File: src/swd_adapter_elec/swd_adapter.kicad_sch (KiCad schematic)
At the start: 2 parts, among them J101 Conn_01x06_Pin, J102 Conn_01x14_Pin

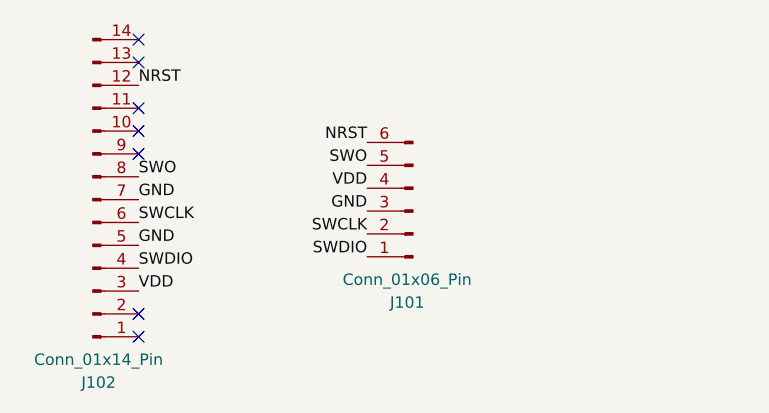
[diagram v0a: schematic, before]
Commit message: The IDC 14 pin to 6 pin converter
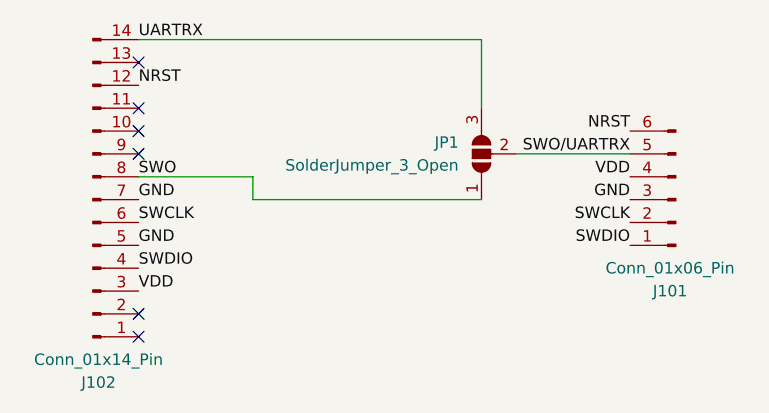
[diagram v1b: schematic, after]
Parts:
- added JP1: SolderJumper_3_Open, Jumper:SolderJumper-3_P1.3mm_Open_RoundedPad1.0x1.5mm, symbol Jumper:SolderJumper_3_Open
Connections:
- net SWO: now also JP1.1 (A); no longer J101.5 (Pin_5)
- net UARTRX: now reaches J102.14 (Pin_14)
- net UARTRX: now also JP1.3 (B)
- new net SWO/UARTRX: J101.5 (Pin_5), JP1.2 (C)
- no-connect marks 7 -> 6
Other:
- moved on the sheet: J101
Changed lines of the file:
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@@
-	)
-	(no_connect
-		(at 63.5 45.72)
 	)
 	(no_connect
 		(at 63.5 58.42)
 	)
+	(wire
+		(pts
+			(xy 105.41 58.42) (xy 118.11 58.42)
+		)
+		(stroke
+			(width 0)
+			(type default)
+		)
+	)
+	(wire
+		(pts
+			(xy 101.6 53.34) (xy 101.6 45.72)
+		)
+		(stroke
+			(width 0)
+			(type default)
+		)
+	)
+	(wire
+		(pts
+			(xy 63.5 45.72) (xy 101.6 45.72)
+		)
+		(stroke
+			(width 0)
+			(type default)
+		)
+	)
+	(wire
+		(pts
+			(xy 101.6 63.5) (xy 76.2 63.5)
+		)
+		(stroke
+			(width 0)
+			(type default)
+		)
+	)
+	(wire
+		(pts
+			(xy 63.5 60.96) (xy 76.2 60.96)
+		)
+		(stroke
+			(width 0)
+			(type default)
+		)
+	)
+	(wire
+		(pts
+			(xy 76.2 63.5) (xy 76.2 60.96)
+		)
+		(stroke
+			(width 0)
+			(type default)
+		)
+	)
 	(label "VDD"
-		(at 88.9 62.23 180)
+		(at 118.11 60.96 180)
 		(effects
 			(font
@@
 		)
 	)
-	(label "SWO"
-		(at 88.9 59.69 180)
+	(label "SWO{slash}UARTRX"
+		(at 118.11 58.42 180)
 		(effects
 			(font
@@
 	)
 	(label "SWCLK"
-		(at 88.9 67.31 180)
+		(at 118.11 66.04 180)
 		(effects
 			(font
@@
 		)
 	)
+	(label "UARTRX"
+		(at 63.5 45.72 0)
+		(effects
+			(font
+				(size 1.27 1.27)
+			)
+			(justify left bottom)
+		)
+	)
 	(label "SWDIO"
 		(at 63.5 71.12 0)
@@
 	)
 	(label "SWDIO"
-		(at 88.9 69.85 180)
+		(at 118.11 68.58 180)
 		(effects
 			(font
@@
 	)
 	(label "NRST"
-		(at 88.9 57.15 180)
+		(at 118.11 55.88 180)
 		(effects
 			(font
@@
 	)
 	(label "GND"
-		(at 88.9 64.77 180)
+		(at 118.11 63.5 180)
 		(effects
 			(font
@@
 	)
 	(symbol
+		(lib_id "Jumper:SolderJumper_3_Open")
+		(at 101.6 58.42 90)
+		(unit 1)
+		(exclude_from_sim no)
+		(in_bom no)
+		(on_board yes)
+		(dnp no)
+		(fields_autoplaced yes)
+		(property "Reference" "JP1"
+			(at 99.06 57.1499 90)
+			(effects
+				(font
+					(size 1.27 1.27)
+				)
+				(justify left)
+			)
+		)
+		(property "Value" "SolderJumper_3_Open"
+			(at 99.06 59.6899 90)
+			(effects
+				(font
+					(size 1.27 1.27)
+				)
+				(justify left)
+			)
+		)
+		(property "Footprint" "Jumper:SolderJumper-3_P1.3mm_Open_RoundedPad1.0x1.5mm"
+			(at 101.6 58.42 0)
+			(effects
+				(font
+					(size 1.27 1.27)
+				)
+				(hide yes)
+			)
+		)
+		(property "Datasheet" "~"
+			(at 101.6 58.42 0)
+			(effects
+				(font
+					(size 1.27 1.27)
+				)
+				(hide yes)
+			)
+		)
+		(property "Description" "Solder Jumper, 3-pole, open"
+			(at 101.6 58.42 0)
+			(effects
+				(font
+					(size 1.27 1.27)
+				)
+				(hide yes)
+			)
+		)
+		(pin "3"
+		)
+		(pin "2"
+		)
+		(pin "1"
+		)
+		(instances
+			(project ""
+				(path "/78f0aa8e-cd0e-4760-a57c-27c4c3b8767a"
+					(reference "JP1")
+					(unit 1)
+				)
+			)
+		)
+	)
+	(symbol
 		(lib_id "Connector:Conn_01x06_Pin")
-		(at 93.98 64.77 180)
+		(at 123.19 63.5 180)
 		(unit 1)
 		(exclude_from_sim no)
@@
 		(dnp no)
 		(property "Reference" "J101"
-			(at 93.345 74.93 0)
+			(at 122.555 73.66 0)
 			(effects
 				(font
@@
 		)
 		(property "Value" "Conn_01x06_Pin"
-			(at 93.345 72.39 0)
+			(at 122.555 71.12 0)
 			(effects
 				(font
@@
 		)
 		(property "Footprint" "Bluesat:IDC6-pad"
-			(at 93.98 64.77 0)
+			(at 123.19 63.5 0)
 			(effects
 				(font
@@
 		)
 		(property "Datasheet" "~"
-			(at 93.98 64.77 0)
+			(at 123.19 63.5 0)
 			(effects
 				(font
@@
 		)
 		(property "Description" "Generic connector, single row, 01x06, script generated"
-			(at 93.98 64.77 0)
-			(effects
-				(font
+			(at 123.19 63.5 0)
+			(effects
+				(font

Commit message: Final touches
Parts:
- J101: footprint Bluesat:IDC6-pad -> Bluesat:IDC6
- J102: footprint Bluesat:IDC14-pad -> Bluesat:IDC14-Plug-Flipped
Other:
- moved on the sheet: J101, J102, JP1
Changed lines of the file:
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@@
 	(paper "A4")
 	(no_connect
-		(at 63.5 48.26)
-	)
-	(no_connect
-		(at 63.5 78.74)
-	)
-	(no_connect
-		(at 63.5 76.2)
-	)
-	(no_connect
-		(at 63.5 53.34)
-	)
-	(no_connect
-		(at 63.5 55.88)
-	)
-	(no_connect
-		(at 63.5 58.42)
-	)
-	(wire
-		(pts
-			(xy 105.41 58.42) (xy 118.11 58.42)
-		)
-		(stroke
-			(width 0)
-			(type default)
-		)
-	)
-	(wire
-		(pts
-			(xy 101.6 53.34) (xy 101.6 45.72)
-		)
-		(stroke
-			(width 0)
-			(type default)
-		)
-	)
-	(wire
-		(pts
-			(xy 63.5 45.72) (xy 101.6 45.72)
-		)
-		(stroke
-			(width 0)
-			(type default)
-		)
-	)
-	(wire
-		(pts
-			(xy 101.6 63.5) (xy 76.2 63.5)
-		)
-		(stroke
-			(width 0)
-			(type default)
-		)
-	)
-	(wire
-		(pts
-			(xy 63.5 60.96) (xy 76.2 60.96)
-		)
-		(stroke
-			(width 0)
-			(type default)
-		)
-	)
-	(wire
-		(pts
-			(xy 76.2 63.5) (xy 76.2 60.96)
+		(at 123.19 81.28)
+	)
+	(no_connect
+		(at 123.19 111.76)
+	)
+	(no_connect
+		(at 123.19 109.22)
+	)
+	(no_connect
+		(at 123.19 86.36)
+	)
+	(no_connect
+		(at 123.19 88.9)
+	)
+	(no_connect
+		(at 123.19 91.44)
+	)
+	(wire
+		(pts
+			(xy 161.29 91.44) (xy 161.29 93.98)
+		)
+		(stroke
+			(width 0)
+			(type default)
+		)
+	)
+	(wire
+		(pts
+			(xy 161.29 93.98) (xy 123.19 93.98)
+		)
+		(stroke
+			(width 0)
+			(type default)
+		)
+	)
+	(wire
+		(pts
+			(xy 165.1 86.36) (xy 177.8 86.36)
+		)
+		(stroke
+			(width 0)
+			(type default)
+		)
+	)
+	(wire
+		(pts
+			(xy 161.29 81.28) (xy 161.29 78.74)
+		)
+		(stroke
+			(width 0)
+			(type default)
+		)
+	)
+	(wire
+		(pts
+			(xy 123.19 78.74) (xy 161.29 78.74)
 		)
 		(stroke
@@
 	)
 	(label "VDD"
-		(at 118.11 60.96 180)
+		(at 177.8 88.9 180)
 		(effects
 			(font
@@
 	)
 	(label "GND"
-		(at 63.5 68.58 0)
+		(at 123.19 101.6 0)
 		(effects
 			(font
@@
 	)
 	(label "SWO{slash}UARTRX"
-		(at 118.11 58.42 180)
+		(at 177.8 86.36 180)
 		(effects
 			(font
@@
 	)
 	(label "SWCLK"
-		(at 118.11 66.04 180)
+		(at 177.8 93.98 180)
 		(effects
 			(font
@@
 	)
 	(label "NRST"
-		(at 63.5 50.8 0)
+		(at 123.19 83.82 0)
 		(effects
 			(font
@@
 	)
 	(label "SWO"
-		(at 63.5 60.96 0)
+		(at 123.19 93.98 0)
 		(effects
 			(font
@@
 	)
 	(label "VDD"
-		(at 63.5 73.66 0)
+		(at 123.19 106.68 0)
 		(effects
 			(font
@@
 	)
 	(label "UARTRX"
-		(at 63.5 45.72 0)
+		(at 123.19 78.74 0)
 		(effects
 			(font
@@
 	)
 	(label "SWDIO"
-		(at 63.5 71.12 0)
+		(at 123.19 104.14 0)
 		(effects
 			(font
@@
 	)
 	(label "SWCLK"
-		(at 63.5 66.04 0)
+		(at 123.19 99.06 0)
 		(effects
 			(font
@@
 	)
 	(label "SWDIO"
-		(at 118.11 68.58 180)
+		(at 177.8 96.52 180)
 		(effects
 			(font
@@
 	)
 	(label "NRST"
-		(at 118.11 55.88 180)
+		(at 177.8 83.82 180)
 		(effects
 			(font
@@
 	)
 	(label "GND"
-		(at 118.11 63.5 180)
+		(at 177.8 91.44 180)
 		(effects
 			(font
@@
 	)
 	(label "GND"
-		(at 63.5 63.5 0)
+		(at 123.19 96.52 0)
 		(effects
 			(font
@@
 	(symbol
 		(lib_id "Jumper:SolderJumper_3_Open")
-		(at 101.6 58.42 90)
+		(at 161.29 86.36 90)
 		(unit 1)
 		(exclude_from_sim no)
@@
 		(fields_autoplaced yes)
 		(property "Reference" "JP1"
-			(at 99.06 57.1499 90)
+			(at 158.75 85.0899 90)
 			(effects
 				(font
@@
 		)
 		(property "Value" "SolderJumper_3_Open"
-			(at 99.06 59.6899 90)
+			(at 158.75 87.6299 90)
 			(effects
 				(font
@@
 		)
 		(property "Footprint" "Jumper:SolderJumper-3_P1.3mm_Open_RoundedPad1.0x1.5mm"
-			(at 101.6 58.42 0)
+			(at 161.29 86.36 0)
 			(effects
 				(font
@@
 		)
 		(property "Datasheet" "~"
-			(at 101.6 58.42 0)
+			(at 161.29 86.36 0)
 			(effects
 				(font
@@
 		)
 		(property "Description" "Solder Jumper, 3-pole, open"
-			(at 101.6 58.42 0)
+			(at 161.29 86.36 0)
 			(effects
 				(font
@@
 	(symbol
 		(lib_id "Connector:Conn_01x06_Pin")
-		(at 123.19 63.5 180)
+		(at 182.88 91.44 180)
 		(unit 1)
 		(exclude_from_sim no)
@@
 		(dnp no)
 		(property "Reference" "J101"
-			(at 122.555 73.66 0)
+			(at 182.245 101.6 0)
 			(effects
 				(font
@@
 		)
 		(property "Value" "Conn_01x06_Pin"
-			(at 122.555 71.12 0)
-			(effects
-				(font
-					(size 1.27 1.27)
-				)
-			)
-		)
-		(property "Footprint" "Bluesat:IDC6-pad"
-			(at 123.19 63.5 0)
+			(at 182.245 99.06 0)
+			(effects
+				(font
+					(size 1.27 1.27)
+				)
+			)
+		)
+		(property "Footprint" "Bluesat:IDC6"
+			(at 182.88 91.44 0)
 			(effects
 				(font
@@
 		)
 		(property "Datasheet" "~"
-			(at 123.19 63.5 0)
+			(at 182.88 91.44 0)
 			(effects
 				(font
@@
 		)
 		(property "Description" "Generic connector, single row, 01x06, script generated"
-			(at 123.19 63.5 0)
+			(at 182.88 91.44 0)
 			(effects
 				(font
@@
 	(symbol
 		(lib_id "Connector:Conn_01x14_Pin")
-		(at 58.42 63.5 0)
+		(at 118.11 96.52 0)
 		(mirror x)
 		(unit 1)
@@
 		(dnp no)
 		(property "Reference" "J102"
-			(at 59.055 83.82 0)
+			(at 118.745 116.84 0)
 			(effects
 				(font
@@
 		)
 		(property "Value" "Conn_01x14_Pin"
-			(at 59.055 81.28 0)
-			(effects
-				(font
-					(size 1.27 1.27)
-				)
-			)
-		)
-		(property "Footprint" "Bluesat:IDC14-pad"
-			(at 58.42 63.5 0)
+			(at 118.745 114.3 0)
+			(effects
+				(font
+					(size 1.27 1.27)
+				)
+			)
+		)
+		(property "Footprint" "Bluesat:IDC14-Plug-Flipped"
+			(at 118.11 96.52 0)
 			(effects
 				(font
@@
 		)
 		(property "Datasheet" "~"
-			(at 58.42 63.5 0)
+			(at 118.11 96.52 0)
 			(effects
 				(font
@@
 		)
 		(property "Description" "Generic connector, single row, 01x14, script generated"
-			(at 58.42 63.5 0)
-			(effects
-				(font
+			(at 118.11 96.52 0)
+			(effects
+				(font

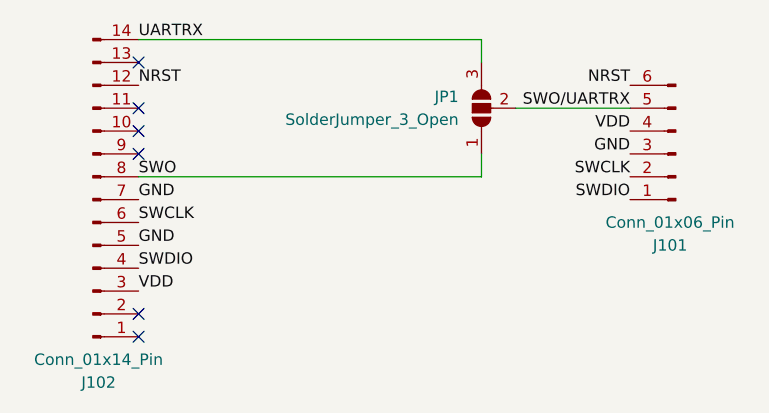
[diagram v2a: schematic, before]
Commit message: Fix IDC6 pinout :sob:, reroute
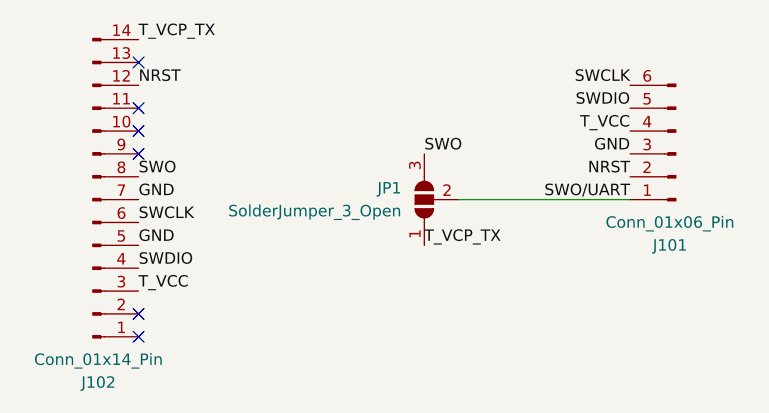
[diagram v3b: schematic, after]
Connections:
- net NRST: now also J101.2 (Pin_2); no longer J101.6 (Pin_6)
- net SWCLK: now also J101.6 (Pin_6); no longer J101.2 (Pin_2)
- net SWDIO: now also J101.5 (Pin_5); no longer J101.1 (Pin_1)
- net SWO: now also JP1.3 (B); no longer JP1.1 (A)
- net SWO/UARTRX renamed SWO/UART
- net SWO/UART: now also J101.1 (Pin_1); no longer J101.5 (Pin_5)
- net UARTRX renamed T_VCP_TX
- net T_VCP_TX: now also JP1.1 (A); no longer JP1.3 (B)
- net VDD renamed T_VCC
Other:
- moved on the sheet: JP1
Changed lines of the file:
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@@
 	(wire
 		(pts
-			(xy 161.29 91.44) (xy 161.29 93.98)
+			(xy 158.75 96.52) (xy 177.8 96.52)
 		)
 		(stroke
@@
 		)
 	)
-	(wire
-		(pts
-			(xy 161.29 93.98) (xy 123.19 93.98)
-		)
-		(stroke
-			(width 0)
-			(type default)
-		)
-	)
-	(wire
-		(pts
-			(xy 165.1 86.36) (xy 177.8 86.36)
-		)
-		(stroke
-			(width 0)
-			(type default)
-		)
-	)
-	(wire
-		(pts
-			(xy 161.29 81.28) (xy 161.29 78.74)
-		)
-		(stroke
-			(width 0)
-			(type default)
-		)
-	)
-	(wire
-		(pts
-			(xy 123.19 78.74) (xy 161.29 78.74)
-		)
-		(stroke
-			(width 0)
-			(type default)
-		)
-	)
-	(label "VDD"
-		(at 177.8 88.9 180)
-		(effects
-			(font
-				(size 1.27 1.27)
-			)
-			(justify right bottom)
-		)
-	)
 	(label "GND"
 		(at 123.19 101.6 0)
@@
 		)
 	)
-	(label "SWO{slash}UARTRX"
+	(label "T_VCP_TX"
+		(at 154.94 101.6 0)
+		(effects
+			(font
+				(size 1.27 1.27)
+			)
+			(justify left bottom)
+		)
+	)
+	(label "SWDIO"
 		(at 177.8 86.36 180)
 		(effects
@@
 		)
 	)
-	(label "SWCLK"
+	(label "NRST"
 		(at 177.8 93.98 180)
 		(effects
@@
 		)
 	)
-	(label "VDD"
+	(label "T_VCC"
+		(at 177.8 88.9 180)
+		(effects
+			(font
+				(size 1.27 1.27)
+			)
+			(justify right bottom)
+		)
+	)
+	(label "T_VCC"
 		(at 123.19 106.68 0)
 		(effects
@@
 		)
 	)
-	(label "UARTRX"
+	(label "T_VCP_TX"
 		(at 123.19 78.74 0)
+		(effects
+			(font
+				(size 1.27 1.27)
+			)
+			(justify left bottom)
+		)
+	)
+	(label "SWO"
+		(at 154.94 91.44 0)
 		(effects
 			(font
@@
 		)
 	)
-	(label "SWDIO"
+	(label "SWO{slash}UART"
 		(at 177.8 96.52 180)
 		(effects
@@
 		)
 	)
-	(label "NRST"
+	(label "SWCLK"
 		(at 177.8 83.82 180)
 		(effects
@@
 	(symbol
 		(lib_id "Jumper:SolderJumper_3_Open")
-		(at 161.29 86.36 90)
+		(at 154.94 96.52 90)
 		(unit 1)
 		(exclude_from_sim no)
@@
 		(fields_autoplaced yes)
 		(property "Reference" "JP1"
-			(at 158.75 85.0899 90)
+			(at 152.4 95.2499 90)
 			(effects
 				(font
@@
 		)
 		(property "Value" "SolderJumper_3_Open"
-			(at 158.75 87.6299 90)
+			(at 152.4 97.7899 90)
 			(effects
 				(font
@@
 		)
 		(property "Footprint" "Jumper:SolderJumper-3_P1.3mm_Open_RoundedPad1.0x1.5mm"
-			(at 161.29 86.36 0)
+			(at 154.94 96.52 0)
 			(effects
 				(font
@@
 		)
 		(property "Datasheet" "~"
-			(at 161.29 86.36 0)
+			(at 154.94 96.52 0)
 			(effects
 				(font
@@
 		)
 		(property "Description" "Solder Jumper, 3-pole, open"
-			(at 161.29 86.36 0)
-			(effects
-				(font
+			(at 154.94 96.52 0)
+			(effects
+				(font
